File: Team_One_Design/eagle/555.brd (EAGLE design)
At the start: 50.8 x 50.8 mm, 9 parts, among them P1 1k, P2 1k

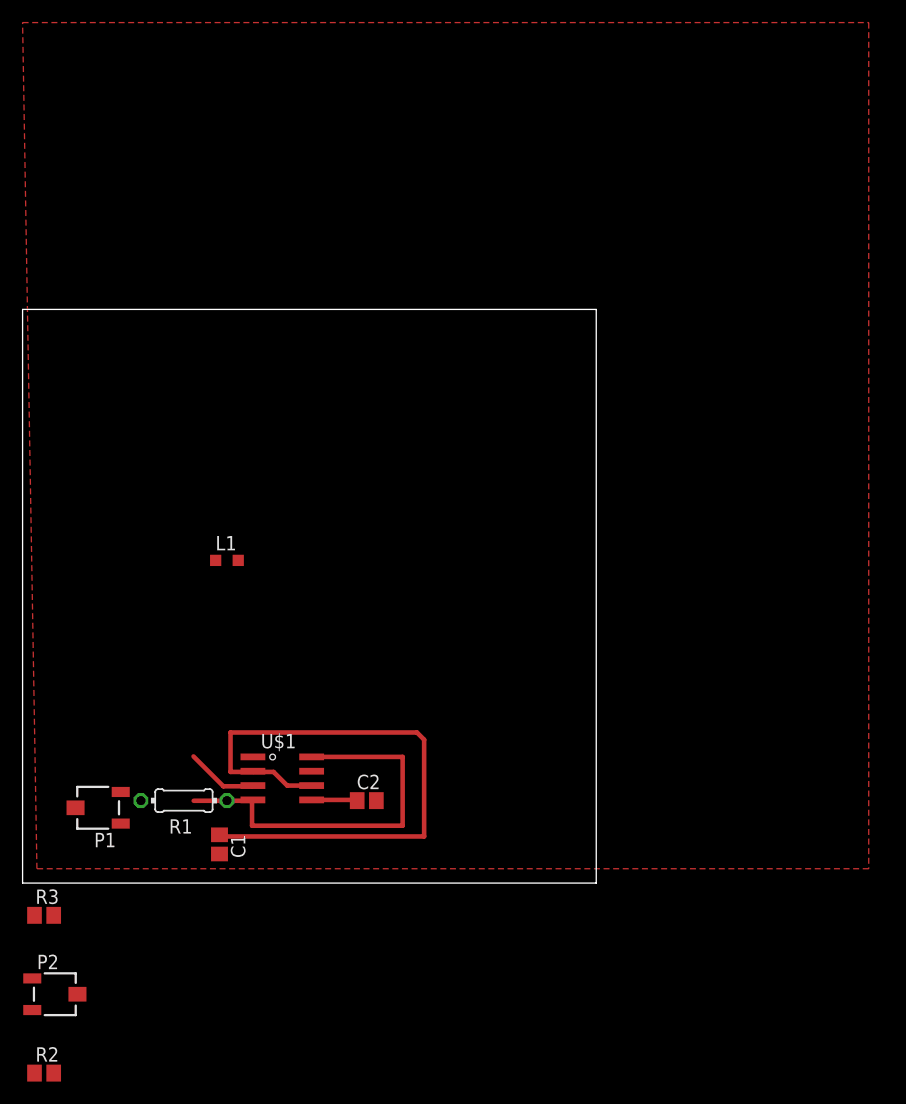
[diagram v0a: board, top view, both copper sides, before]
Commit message: added datasheet for new RF diode, updated schem and layout for 555 circuit.
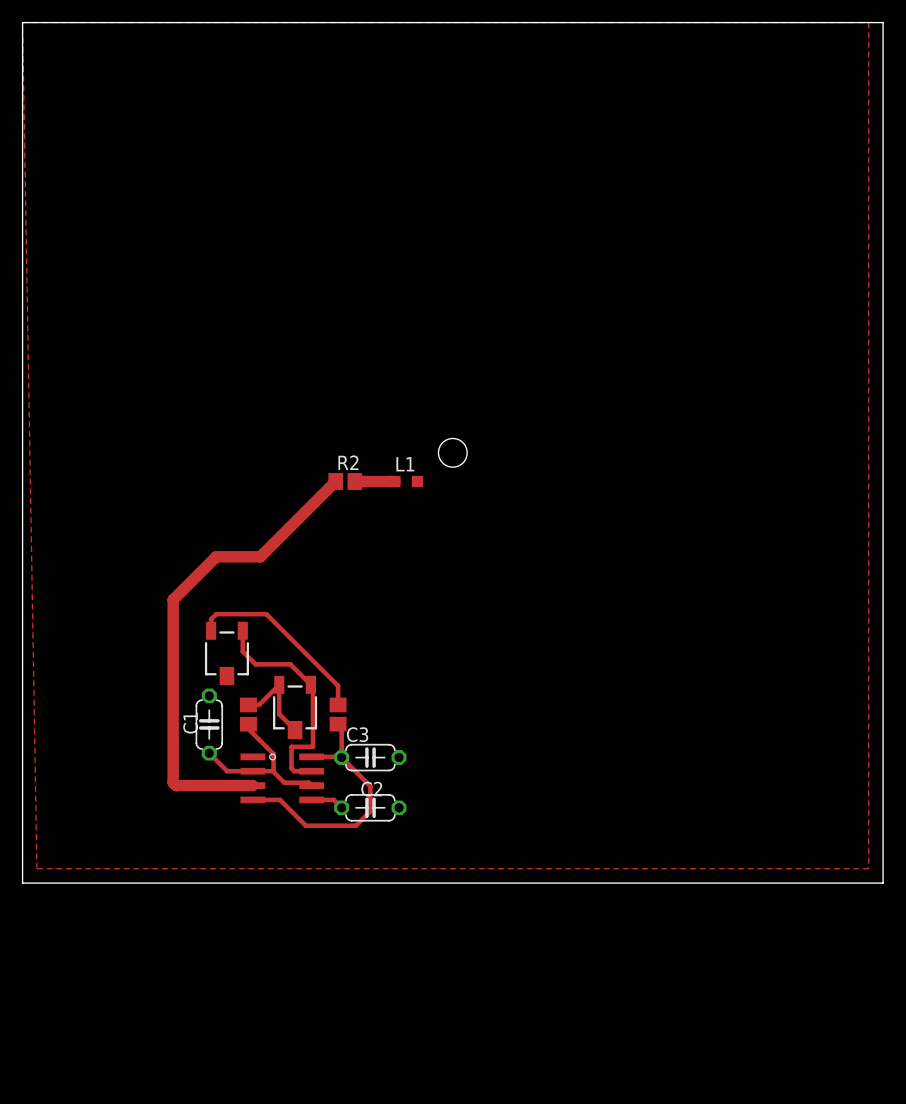
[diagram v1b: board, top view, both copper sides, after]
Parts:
- removed R1: 100k, resistor:0204/7
- removed R3: 1.8k, resistor:R0805
- added C3: 0.1uF, resistor:C050-024X044
- added RA, RB: xxx, resistor:R0805
- C1, C2: device resistor:C0805 -> resistor:C050-024X044
- R2: value 1.8k -> 1.5k
- moved R2 58.8 mm to (28.6, 35.6)
- moved P2 33.1 mm to (24.1, 15.6), turned to 270 degrees
- moved P1 17.8 mm to (18.1, 20.3), turned to 270 degrees
- moved L1 17.3 mm to (34.0, 35.6)
- moved C1 10.7 mm to (16.5, 14.0), turned to 90 degrees
- moved C2 0.71 mm to (30.8, 6.67)
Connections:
- net GND: now also C3.2
- net N$4: now also RB.1; no longer R3.1
- net N$5: now also RB.2; no longer R3.2
- net N$6: now also RA.2; no longer R1.1
- net VCC: now also C3.1, RA.1; no longer R1.2
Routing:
- net N$4: track 55.1 -> 15.4 mm
- net N$2: track 6.38 -> 42.1 mm
- net N$1: track 0.00 -> 20.3 mm
- net N$6: track 0.00 -> 16.8 mm
- net VCC: track 35.0 -> 23.5 mm
- net N$5: track 0.00 -> 8.05 mm
- net N$8: track 0.00 -> 3.55 mm
- net N$7: track 4.10 -> 2.95 mm
- net GND: track 0.00 -> 0.77 mm
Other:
- board size 50.8 x 50.8 mm -> 76.2 x 76.2 mm

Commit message: updated schematic and layout of 555 timer board
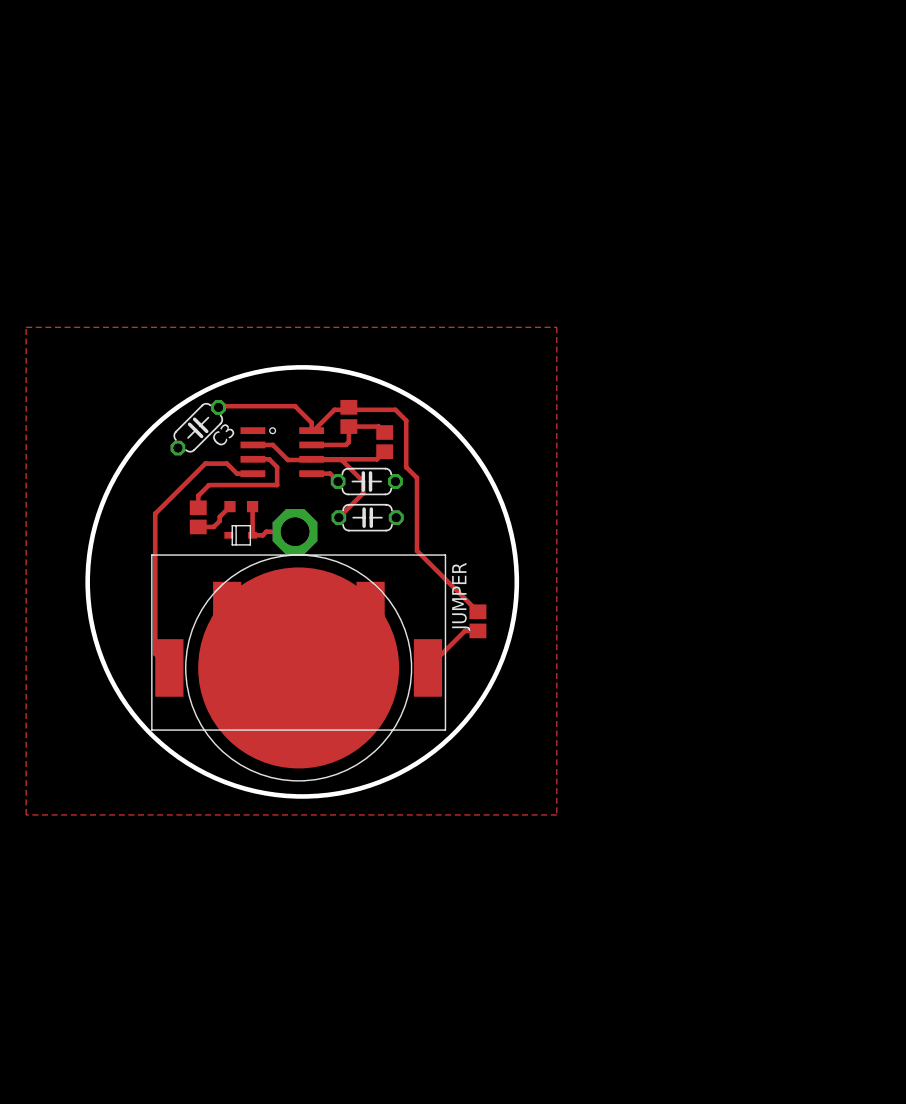
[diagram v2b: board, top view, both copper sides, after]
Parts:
- removed P1, P2: 1k, potentiometer:3223J
- added ANT1: (no value), discrete:PAD-01
- added JUMPER: 0, resistor:R0805
- added U$2: BAT_HOLDER, ece510_library:BAT_HOLDER
- added U$3: BAT-15-03W, ece510_library:BAT-15-03W
- moved C3 32.9 mm to (15.6, 40.3), turned to 225 degrees
- moved C2 28.9 mm to (30.5, 35.6)
- moved U$1 28.9 mm to (23.3, 38.5)
- moved RB 27.0 mm to (32.1, 39.1)
- moved RA 26.4 mm to (28.9, 41.3), turned to 270 degrees
- moved C1 23.1 mm to (30.5, 32.4), turned to 0 degrees
- moved L1 14.8 mm to (19.4, 33.3)
- moved R2 13.4 mm to (15.6, 32.4), turned to 270 degrees
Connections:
- removed net N$5: P2.2, P2.3, RB.2
- removed net N$6: P1.3, RA.2
- new net N$9: ANT1.1, L1.2, U$3.A
- net GND: now also U$2.P_G2, U$2.P_G3, U$2.P_GND, U$3.C
- net N$1: now also RA.2, RB.2; no longer P1.1, P2.1
- net N$3: now also JUMPER.1, U$1.4, U$2.P_+; no longer P1.2
- net VCC: now also JUMPER.2; no longer U$1.4
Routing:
- net N$3: track 0.00 -> 31.0 mm
- net N$2: track 42.1 -> 12.5 mm
- net N$6: track 16.8 -> 0.00 mm
- net VCC: track 23.5 -> 39.0 mm
- net N$1: track 20.3 -> 8.17 mm
- net N$5: track 8.05 -> 0.00 mm
- net N$4: track 15.4 -> 22.0 mm
- net N$9: track 0.00 -> 6.43 mm
- net GND: track 0.77 -> 0.00 mm
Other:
- board size 76.2 x 76.2 mm -> 38 x 38 mm
